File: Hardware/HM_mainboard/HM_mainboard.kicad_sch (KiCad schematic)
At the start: 0 parts

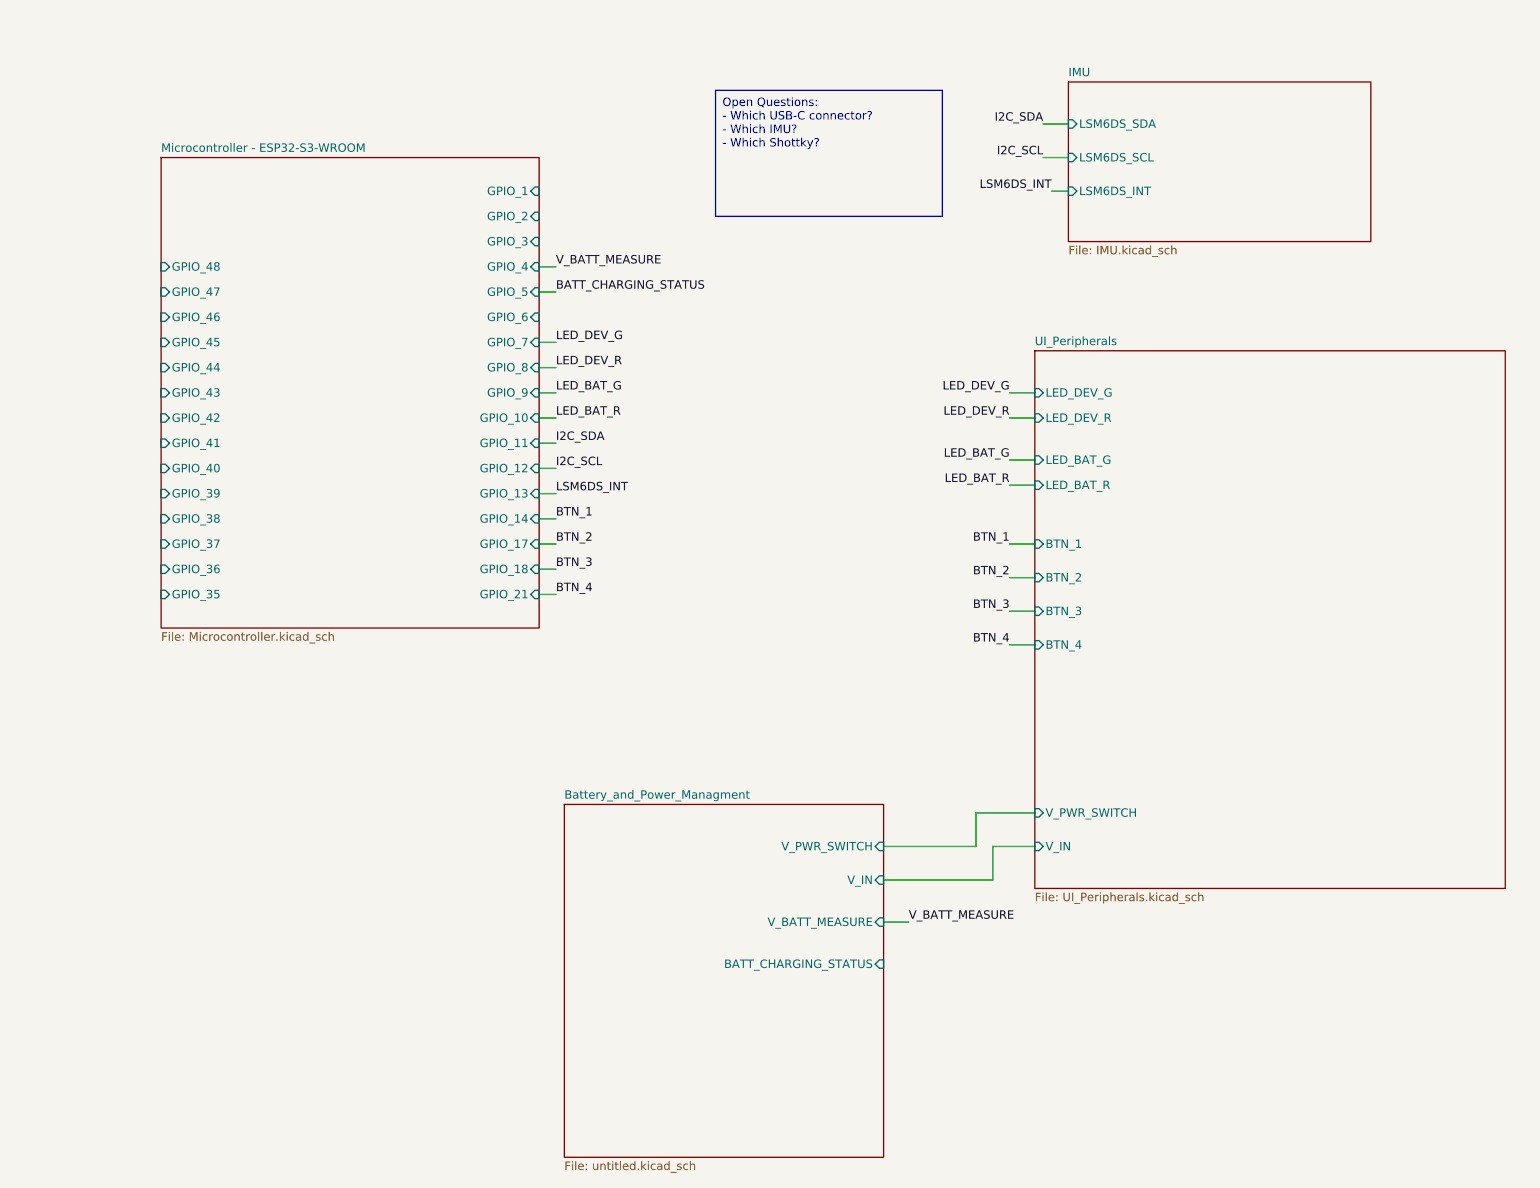
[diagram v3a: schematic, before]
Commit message: Changed I2C address selection of IMUs
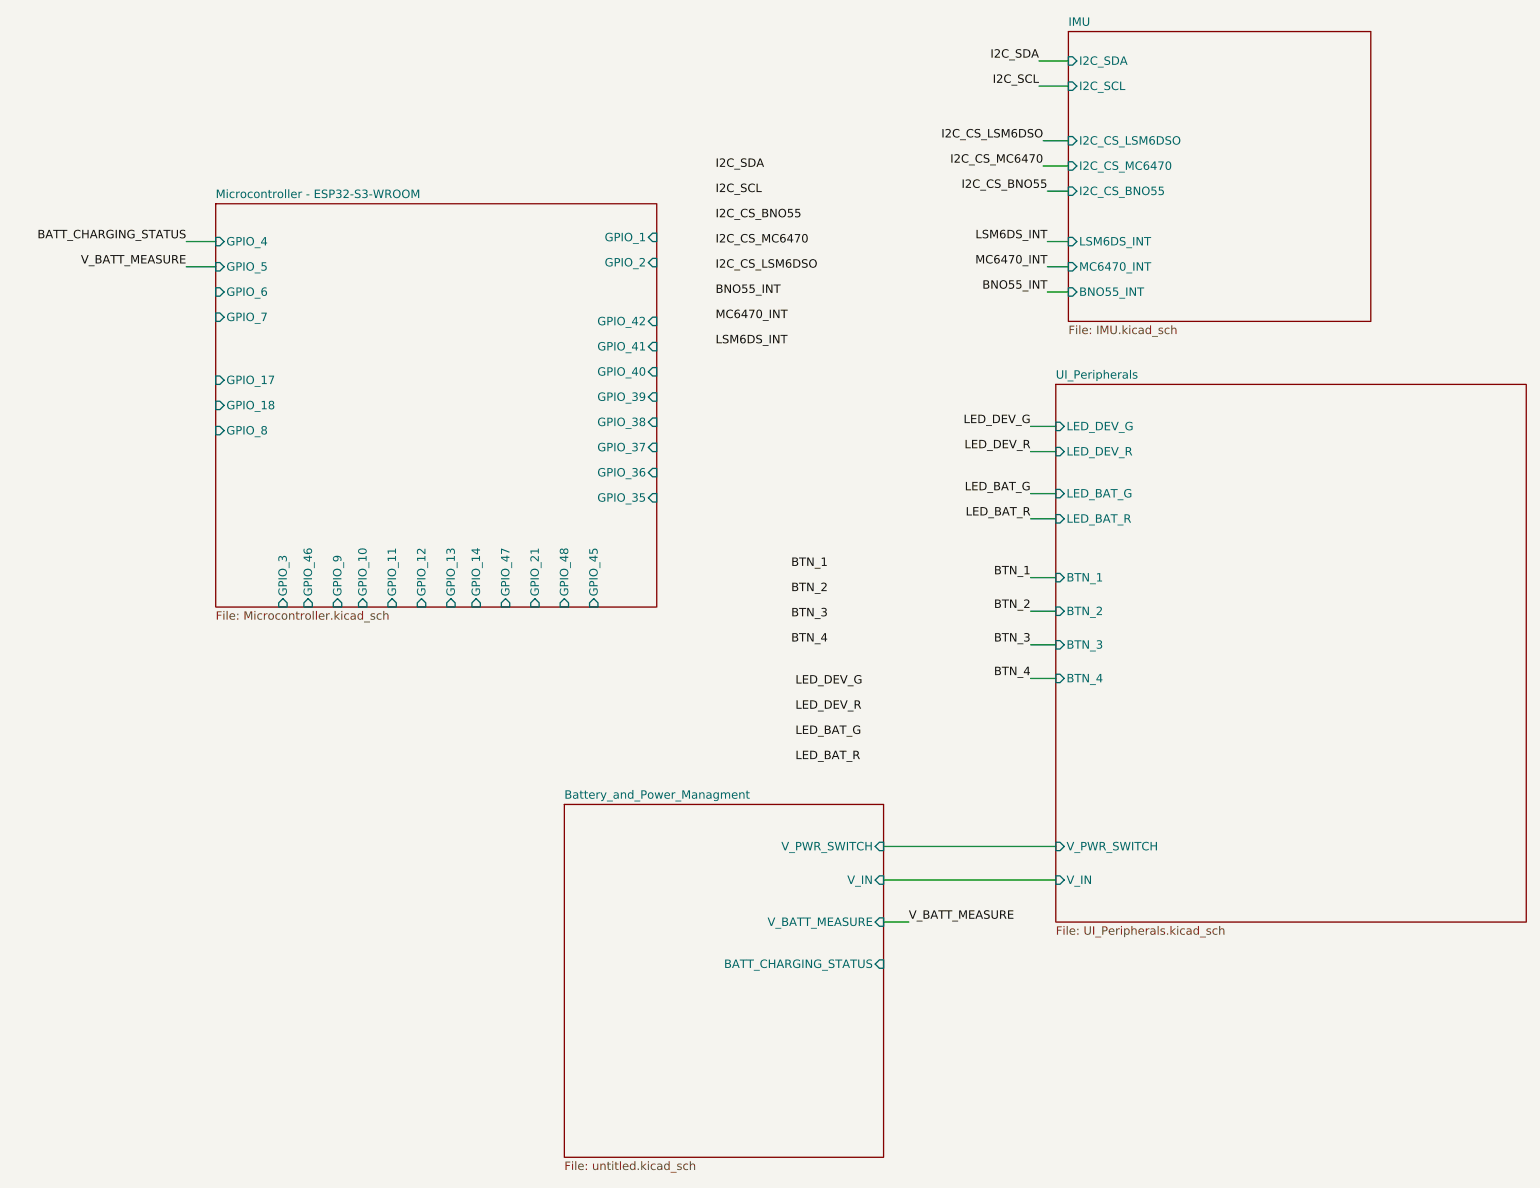
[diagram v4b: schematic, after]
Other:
- sheet IMU ports: added BNO55_INT, I2C_CS_BNO55, I2C_CS_LSM6DSO, I2C_CS_MC6470, I2C_SCL, I2C_SDA, MC6470_INT; removed LSM6DS_SCL, LSM6DS_SDA
- sheet Microcontroller - ESP32-S3-WROOM ports: added none; removed GPIO_43, GPIO_44

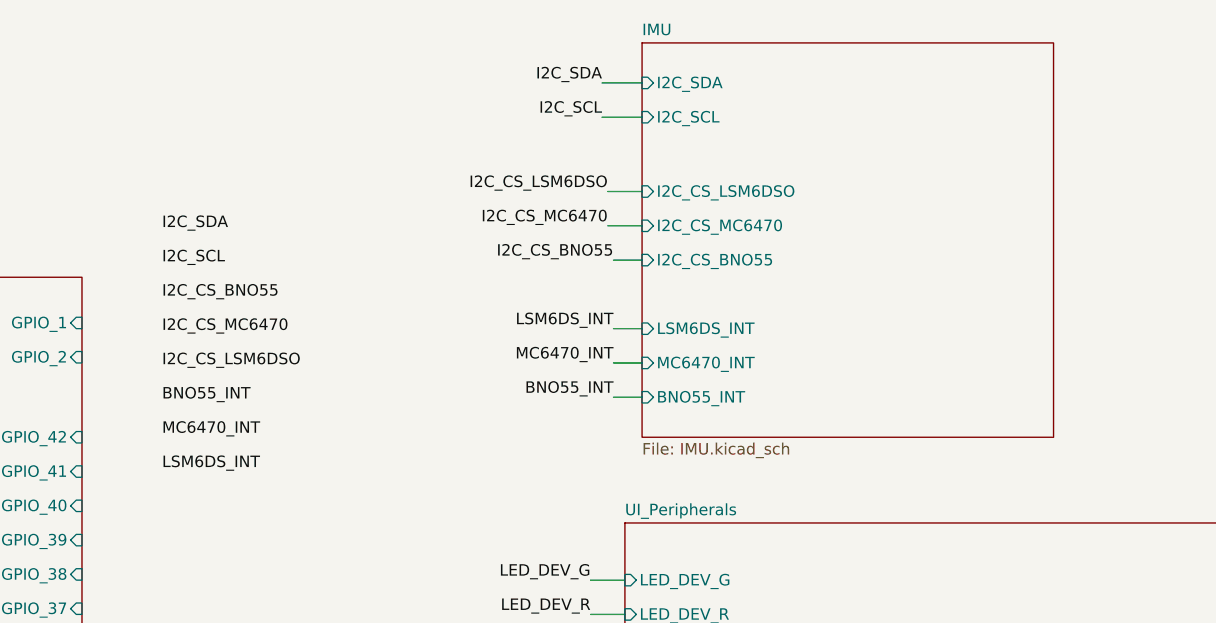
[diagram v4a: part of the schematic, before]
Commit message: Added pull-ups to i2c connections
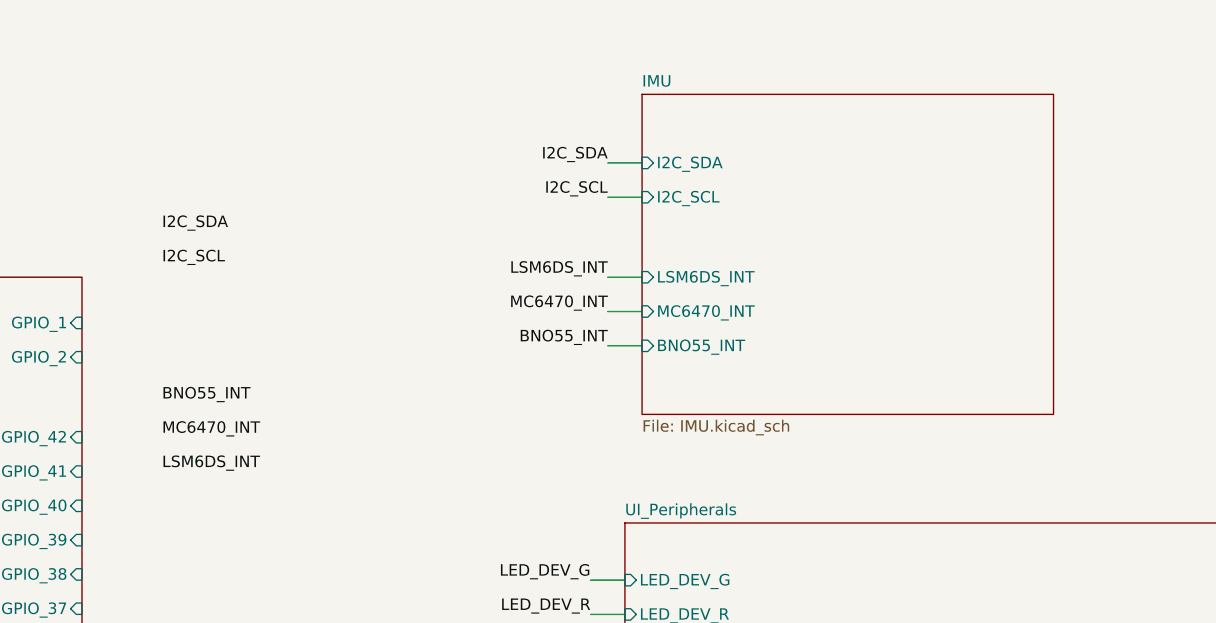
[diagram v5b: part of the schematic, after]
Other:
- sheet IMU ports: added none; removed I2C_CS_BNO55, I2C_CS_LSM6DSO, I2C_CS_MC6470
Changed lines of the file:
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@@
     (stroke (width 0) (type default))
   )
-  (wire (pts (xy 175.895 48.26) (xy 179.07 48.26))
+  (wire (pts (xy 175.26 42.545) (xy 179.07 42.545))
     (stroke (width 0) (type default))
   )
@@
     (stroke (width 0) (type default))
   )
-  (wire (pts (xy 174.625 24.765) (xy 179.07 24.765))
+  (wire (pts (xy 175.26 33.655) (xy 179.07 33.655))
     (stroke (width 0) (type default))
   )
@@
     (stroke (width 0) (type default))
   )
-  (wire (pts (xy 175.26 33.02) (xy 179.07 33.02))
-    (stroke (width 0) (type default))
-  )
-  (wire (pts (xy 175.895 55.88) (xy 179.07 55.88))
+  (wire (pts (xy 175.26 50.165) (xy 179.07 50.165))
     (stroke (width 0) (type default))
   )
@@
     (stroke (width 0) (type default))
   )
-  (wire (pts (xy 175.26 36.83) (xy 179.07 36.83))
-    (stroke (width 0) (type default))
-  )
   (wire (pts (xy 173.355 114.3) (xy 177.165 114.3))
     (stroke (width 0) (type default))
   )
-  (wire (pts (xy 175.895 52.07) (xy 179.07 52.07))
+  (wire (pts (xy 175.26 46.355) (xy 179.07 46.355))
     (stroke (width 0) (type default))
   )
@@
     (stroke (width 0) (type default))
   )
-  (wire (pts (xy 175.895 40.64) (xy 179.07 40.64))
-    (stroke (width 0) (type default))
-  )
-  (wire (pts (xy 174.625 20.955) (xy 179.07 20.955))
+  (wire (pts (xy 175.26 29.845) (xy 179.07 29.845))
     (stroke (width 0) (type default))
   )
@@
     (effects (font (size 1.27 1.27)) (justify right bottom))
   )
-  (label "I2C_CS_MC6470" (at 175.26 36.83 180) (fields_autoplaced)
-    (effects (font (size 1.27 1.27)) (justify right bottom))
-  )
   (label "LED_DEV_R" (at 137.795 119.38 0) (fields_autoplaced)
     (effects (font (size 1.27 1.27)) (justify left bottom))
@@
     (effects (font (size 1.27 1.27)) (justify right bottom))
   )
-  (label "I2C_CS_LSM6DSO" (at 175.26 33.02 180) (fields_autoplaced)
-    (effects (font (size 1.27 1.27)) (justify right bottom))
-  )
-  (label "I2C_CS_LSM6DSO" (at 125.73 52.705 0) (fields_autoplaced)
-    (effects (font (size 1.27 1.27)) (justify left bottom))
-  )
   (label "BTN_3" (at 137.16 105.41 0) (fields_autoplaced)
     (effects (font (size 1.27 1.27)) (justify left bottom))
   )
-  (label "I2C_CS_BNO55" (at 125.73 45.085 0) (fields_autoplaced)
-    (effects (font (size 1.27 1.27)) (justify left bottom))
-  )
   (label "BTN_1" (at 173.355 99.06 180) (fields_autoplaced)
     (effects (font (size 1.27 1.27)) (justify right bottom))
@@
     (effects (font (size 1.27 1.27)) (justify left bottom))
   )
-  (label "I2C_CS_BNO55" (at 175.895 40.64 180) (fields_autoplaced)
-    (effects (font (size 1.27 1.27)) (justify right bottom))
-  )
   (label "BNO55_INT" (at 125.73 56.515 0) (fields_autoplaced)
     (effects (font (size 1.27 1.27)) (justify left bottom))
   )
-  (label "I2C_SDA" (at 174.625 20.955 180) (fields_autoplaced)
+  (label "I2C_SDA" (at 175.26 29.845 180) (fields_autoplaced)
     (effects (font (size 1.27 1.27)) (justify right bottom))
   )
@@
     (effects (font (size 1.27 1.27)) (justify right bottom))
   )
-  (label "I2C_CS_MC6470" (at 125.73 48.895 0) (fields_autoplaced)
-    (effects (font (size 1.27 1.27)) (justify left bottom))
-  )
-  (label "LSM6DS_INT" (at 175.895 48.26 180) (fields_autoplaced)
+  (label "LSM6DS_INT" (at 175.26 42.545 180) (fields_autoplaced)
     (effects (font (size 1.27 1.27)) (justify right bottom))
   )
@@
     (effects (font (size 1.27 1.27)) (justify left bottom))
   )
-  (label "MC6470_INT" (at 175.895 52.07 180) (fields_autoplaced)
+  (label "MC6470_INT" (at 175.26 46.355 180) (fields_autoplaced)
     (effects (font (size 1.27 1.27)) (justify right bottom))
   )
@@
     (effects (font (size 1.27 1.27)) (justify left bottom))
   )
-  (label "BNO55_INT" (at 175.895 55.88 180) (fields_autoplaced)
-    (effects (font (size 1.27 1.27)) (justify right bottom))
-  )
-  (label "I2C_SCL" (at 174.625 24.765 180) (fields_autoplaced)
+  (label "BNO55_INT" (at 175.26 50.165 180) (fields_autoplaced)
+    (effects (font (size 1.27 1.27)) (justify right bottom))
+  )
+  (label "I2C_SCL" (at 175.26 33.655 180) (fields_autoplaced)
     (effects (font (size 1.27 1.27)) (justify right bottom))
   )
@@
     )
   )
-  (sheet (at 179.07 16.51) (size 45.72 43.815) (fields_autoplaced)
+  (sheet (at 179.07 22.225) (size 45.72 35.56) (fields_autoplaced)
     (stroke (width 0.1524) (type solid))
     (fill (color 0 0 0 0.0000))
-    (property "Sheetname" "IMU" (at 179.07 15.7984 0)
+    (property "Sheetname" "IMU" (at 179.07 21.5134 0)
       (effects (font (size 1.27 1.27)) (justify left bottom))
     )
-    (property "Sheetfile" "IMU.kicad_sch" (at 179.07 60.9096 0)
+    (property "Sheetfile" "IMU.kicad_sch" (at 179.07 58.3696 0)
       (effects (font (size 1.27 1.27)) (justify left top))
     )
-    (pin "LSM6DS_INT" input (at 179.07 48.26 180)
-      (effects (font (size 1.27 1.27)) (justify left))
-    )
-    (pin "I2C_CS_BNO55" input (at 179.07 40.64 180)
-      (effects (font (size 1.27 1.27)) (justify left))
-    )
-    (pin "I2C_SCL" input (at 179.07 24.765 180)
-      (effects (font (size 1.27 1.27)) (justify left))
-    )
-    (pin "I2C_SDA" input (at 179.07 20.955 180)
-      (effects (font (size 1.27 1.27)) (justify left))
-    )
-    (pin "BNO55_INT" input (at 179.07 55.88 180)
-      (effects (font (size 1.27 1.27)) (justify left))
-    )
-    (pin "I2C_CS_LSM6DSO" input (at 179.07 33.02 180)
-      (effects (font (size 1.27 1.27)) (justify left))
-    )
-    (pin "I2C_CS_MC6470" input (at 179.07 36.83 180)
-      (effects (font (size 1.27 1.27)) (justify left))
-    )
-    (pin "MC6470_INT" input (at 179.07 52.07 180)
-      (effects (font (size 1.27 1.27)) (justify left))
-    )
+    (pin "LSM6DS_INT" input (at 179.07 42.545 180)
+      (effects (font (size 1.27 1.27)) (justify left))
+    )
+    (pin "I2C_SCL" input (at 179.07 33.655 180)
+      (effects (font (size 1.27 1.27)) (justify left))
+    )
+    (pin "I2C_SDA" input (at 179.07 29.845 180)
+      (effects (font (size 1.27 1.27)) (justify left))
+    )
+    (pin "BNO55_INT" input (at 179.07 50.165 180)
+      (effects (font (size 1.27 1.27)) (justify left))
+    )
+    (pin "MC6470_INT" input (at 179.07 46.355 180)
+      (effects (font (size 1.27 1.27)) (justify left))
+    )
